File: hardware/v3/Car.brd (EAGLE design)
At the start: 80 x 53.3 mm, 75 parts, among them IC1 PIC24FJ64GB204, IC2 LD117AS50TR, IC3 LD117AS33TR

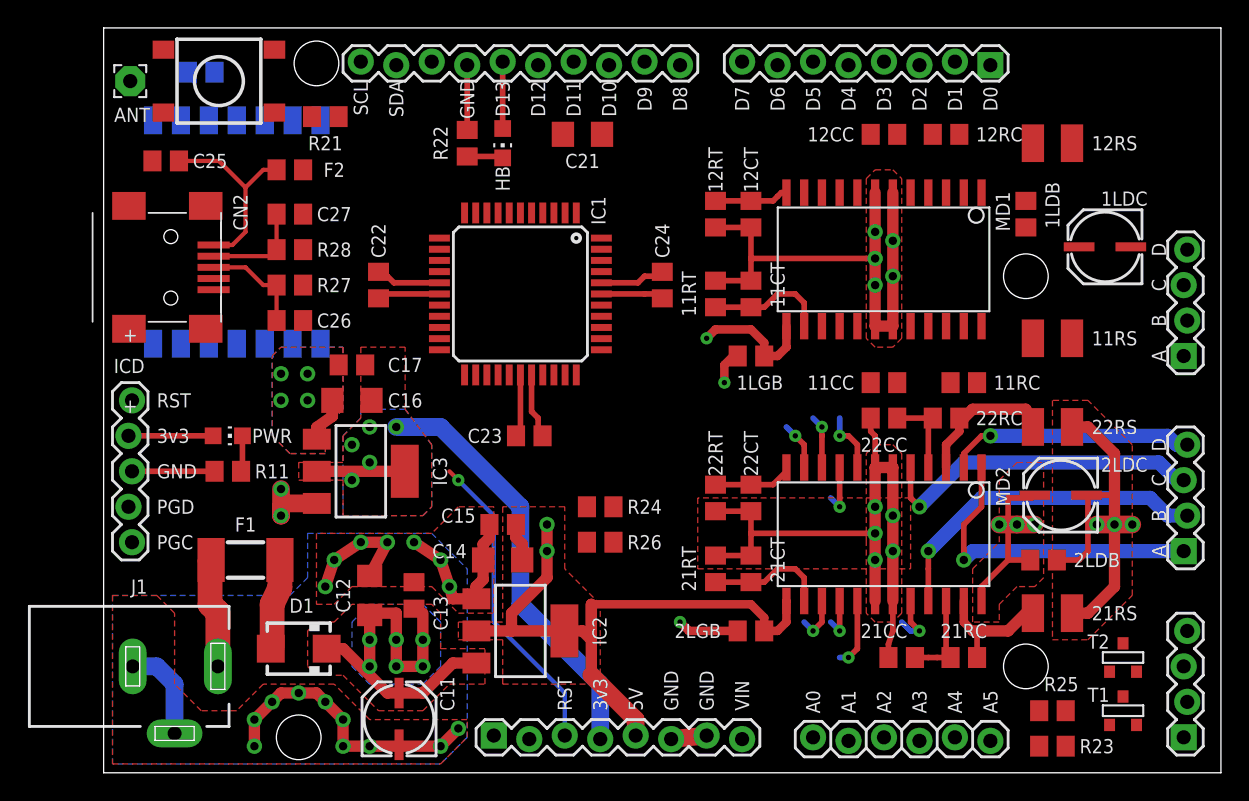
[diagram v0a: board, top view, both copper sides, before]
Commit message: Finished routing power for motor driver 1.
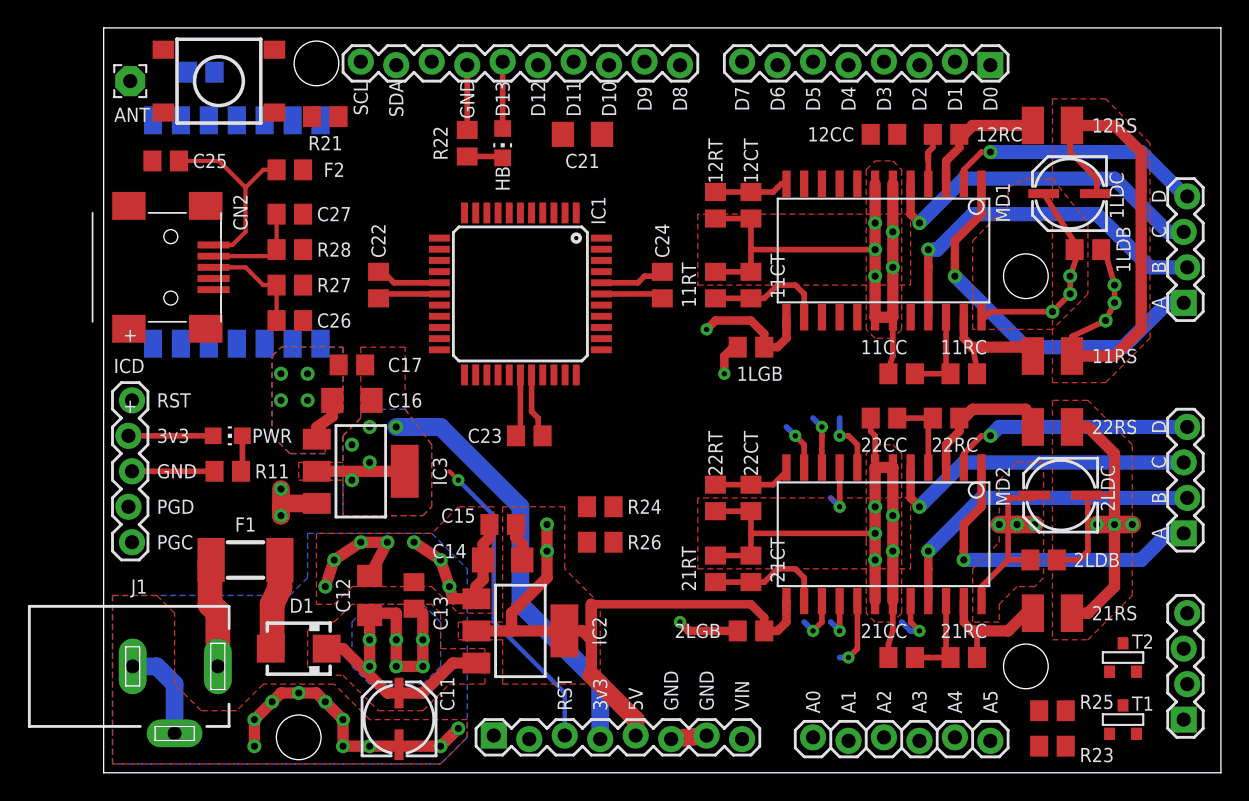
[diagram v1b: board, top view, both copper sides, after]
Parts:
- 11RS, 21RS: value 1 -> 0.5
- moved 1LDB 5.12 mm to (70.5, 37.5), turned to 0 degrees
- moved 1LDC 4.58 mm to (69.2, 41.3)
- moved M1 3.81 mm to (77.5, 33.7)
- moved 11CC 1.42 mm to (57.1, 28.6)
- moved JP1 1.27 mm to (77.5, 3.81)
- moved 11RS 1.27 mm to (67.9, 29.8)
- moved M2 1.27 mm to (77.5, 17.1)
- moved 12RS 1.27 mm to (67.9, 46.4)
- moved MD1 0.64 mm to (55.9, 37.5)
- moved 1LGB 0.64 mm to (46.4, 30.5)
- moved T1 0.64 mm to (73.0, 3.81)
- moved 11CT 0.63 mm to (46.4, 34.9)
- moved 11RC 0.63 mm to (61.6, 28.6)
- moved 11RT 0.63 mm to (43.8, 34.9)
- moved 12CT 0.63 mm to (46.4, 40.6)
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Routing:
- net GND: track 453.9 -> 499.4 mm, vias 36 -> 39
- net N$2: track 0.00 -> 27.2 mm, vias 0 -> 1
- net N$1: track 0.00 -> 26.0 mm, vias 0 -> 1
- net N$4: track 0.00 -> 24.9 mm, vias 0 -> 1
- net N$5: track 0.00 -> 19.0 mm, vias 0 -> 1
- net VIN: track 166.0 -> 179.2 mm, vias 9 -> 12
- net N$35: track 0.00 -> 9.46 mm
- net N$31: track 0.00 -> 8.96 mm
- net N$33: track 0.00 -> 7.36 mm
- net N$34: track 0.00 -> 4.30 mm
- net +5V: track 114.2 -> 114.8 mm
- net N$9: track 23.8 -> 23.3 mm
- net N$8: track 23.2 -> 23.7 mm
- net N$6: track 24.2 -> 23.7 mm

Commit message: Finished routing power lines and other significant signals.
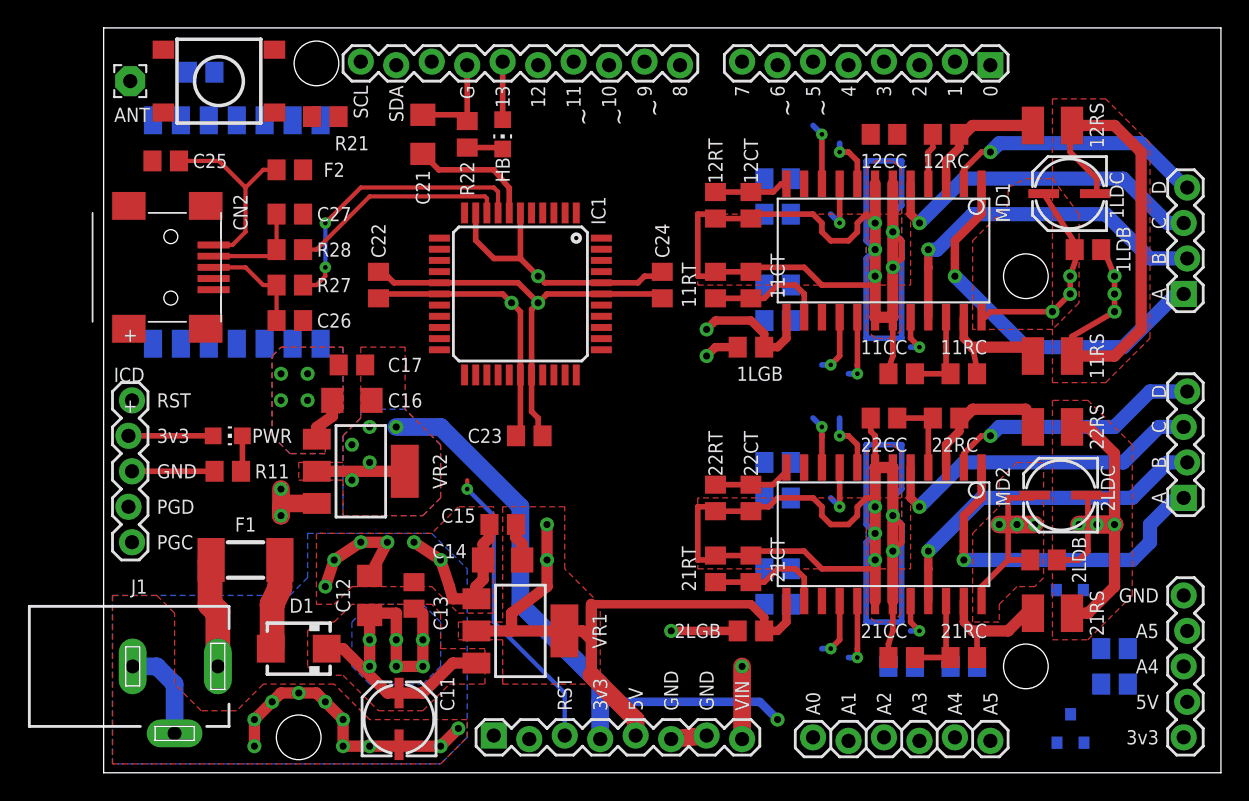
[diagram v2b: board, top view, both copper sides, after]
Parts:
- removed JP1: (no value), SparkFun-Connectors:1X04_LOCK
- added C31, C32, C33, C34: 1n, rcl:C0805
- added PIO: (no value), SparkFun-Connectors:1X05_LOCK
- added R31, R32, R33, R34: 2k, rcl:R0805
- 12RS, 22RS: value 1 -> 0.5
- R23, R25: value 1k -> 10k
- T1, T2: value (none) -> 2N3904
- moved R24 39.0 mm to (72.4, 6.35), flipped to the bottom
- moved R26 37.6 mm to (72.4, 8.89), flipped to the bottom
- moved R23 12.2 mm to (57.1, 7.62), flipped to the bottom, turned to 180 degrees
- moved C21 11.4 mm to (22.9, 45.7), turned to 90 degrees
- moved R25 7.10 mm to (61.6, 7.62), flipped to the bottom, turned to 180 degrees
- moved T2 5.39 mm to (69.2, 12.1), flipped to the bottom, turned to 0 degrees
- moved T1 3.86 mm to (69.2, 3.17), flipped to the bottom
- moved M2 2.54 mm to (77.5, 19.7)
- moved HB 0.63 mm to (28.6, 45.7)
- moved M1 0.63 mm to (77.5, 34.3)
- moved R22 0.63 mm to (26.0, 45.7)
- renumbered IC2 to VR1, IC3 to VR2, JP6 to PWR_IN, JP7 to DIO1, JP8 to DIO2, JP9 to AIO
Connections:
- new net M1_VREF1: C31.1, MD1.15, R31.2
- new net M1_VREF2: C32.1, MD1.11, R32.2
- new net M2_VREF1: C33.1, MD2.15, R33.2
- new net M2_VREF2: C34.1, MD2.11, R34.2
- net +3V3: now also PIO.1
- net +5V: now also PIO.2; no longer JP1.1, R24.2, R26.2
- net A4_PO: now also PIO.3, R24.2; no longer JP1.2, T1.2
- net A5_PO: now also PIO.4, R26.2; no longer JP1.3, T2.2
- net D10/M2_PWM2: now also R34.1; no longer MD2.11
- net D5/M1_PWM1: now also R31.1; no longer MD1.15
- net D6/M1_PWM2: now also R32.1; no longer MD1.11
- net D9/M2_PWM1: now also R33.1; no longer MD2.15
- net GND: now also C31.2, C32.2, C33.2, C34.2, PIO.5, T1.2, T2.2; no longer JP1.4
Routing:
- net GND: track 499.4 -> 695.5 mm
- net +3V3: track 72.6 -> 161.5 mm, vias 5 -> 8
- net +5V: track 114.8 -> 153.4 mm
- net USBD+: track 0.00 -> 20.7 mm, vias 0 -> 2
- net USBD-: track 0.00 -> 15.8 mm
- net N$40: track 0.00 -> 9.05 mm
- net M1_I11: track 0.00 -> 4.68 mm, vias 0 -> 1
- net D3/M1_P2: track 0.00 -> 4.44 mm, vias 0 -> 1
- net D2/M1_P1: track 0.00 -> 4.31 mm, vias 0 -> 1
- net VIN: track 179.2 -> 183.4 mm, vias 12 -> 13
- net M1_I02: track 0.00 -> 3.80 mm, vias 0 -> 1
- net M1_I12: track 0.00 -> 3.71 mm, vias 0 -> 1
- net D10/M2_PWM2: track 3.43 -> 0.00 mm, vias 1 -> 0
- net D9/M2_PWM1: track 3.30 -> 0.00 mm, vias 1 -> 0
- net M1_I01: track 0.00 -> 3.04 mm, vias 0 -> 1
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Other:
- board text added: "0"
- board text added: "1"
- board text added: "10"
- board text added: "11"
- board text added: "12"
- board text added: "13"
- board text added: "2"
- board text added: "3"
- board text added: "4"
- board text added: "5"
- board text added: "6"
- board text added: "7"
- board text added: "8"
- board text added: "9"
- board text added: "G"
- board text added: "~"
- board text removed: "D0"
- board text removed: "D1"
- board text removed: "D10"
- board text removed: "D11"
- board text removed: "D12"
- board text removed: "D13"
- board text removed: "D2"
- board text removed: "D3"
- board text removed: "D4"
- board text removed: "D5"
- board text removed: "D6"
- board text removed: "D7"
- board text removed: "D8"
- board text removed: "D9"

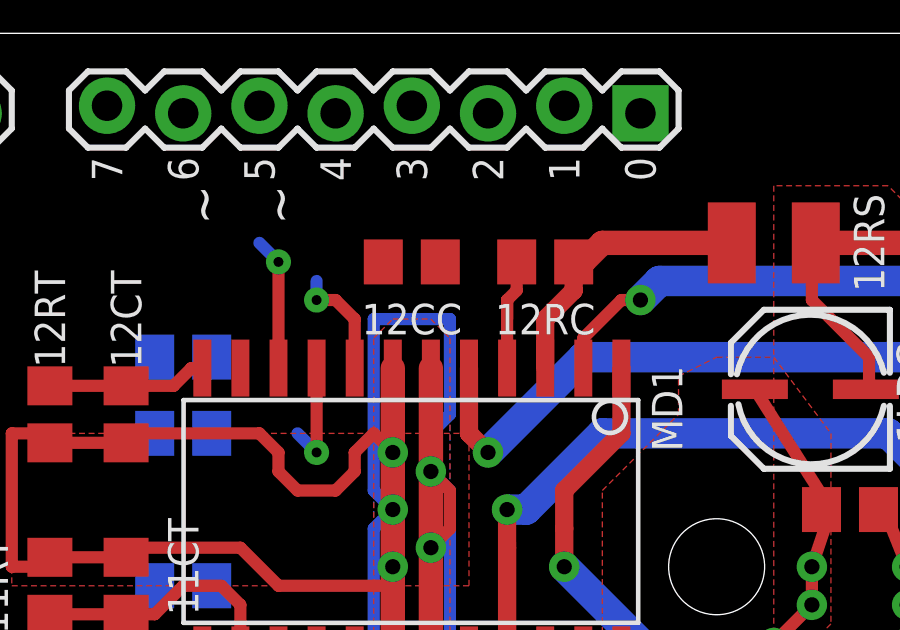
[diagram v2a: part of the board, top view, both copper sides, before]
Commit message: Fixed some part values. Cleaned up schematic and board names/values.
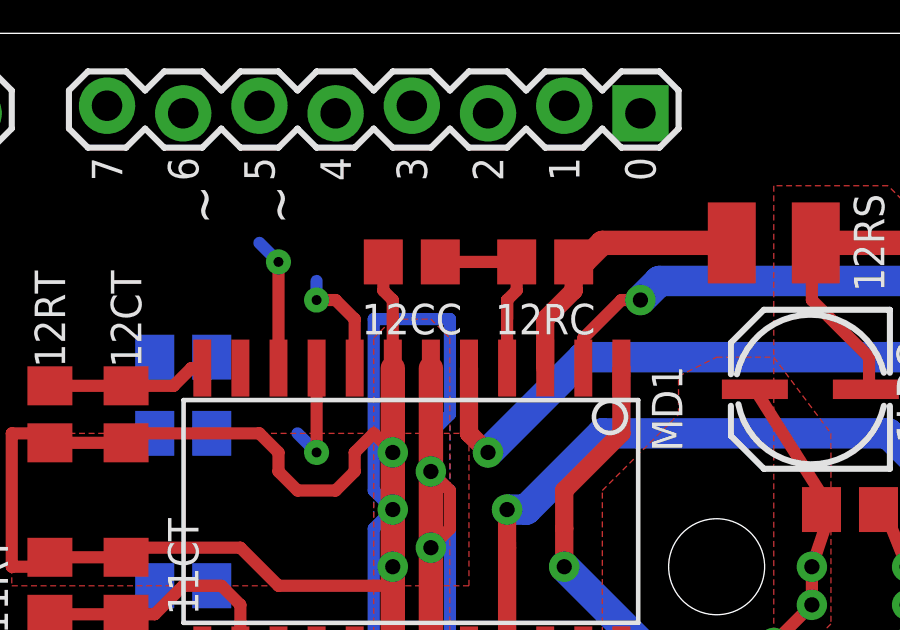
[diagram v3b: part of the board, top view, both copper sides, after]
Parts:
- C31, C32, C33, C34: value 1n -> 100n
- R31, R32, R33, R34: value 2k -> 10k
- renumbered MOUTH to IC2
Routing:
- net GND: track 695.5 -> 699.1 mm
- net N$34: track 4.30 -> 6.85 mm
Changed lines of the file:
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@@
 <attribute name="VALUE" x="47.625" y="33.02" size="1.016" layer="27" rot="R180" align="center"/>
 </element>
-<element name="MOUTH" library="SparkFun-RF" package="RFM12-XXX-S2" value="RFM12" x="9.525" y="38.735" smashed="yes" rot="MR90">
+<element name="IC2" library="SparkFun-RF" package="RFM12-XXX-S2" value="RFM12" x="9.525" y="38.735" smashed="yes" rot="MR90">
 <attribute name="VALUE" x="5.535" y="43.725" size="1.016" layer="28" rot="MR270" align="center"/>
 <attribute name="NAME" x="18.775" y="38.645" size="1.016" layer="26" rot="MR270" align="center"/>
@@
 <attribute name="VALUE" x="80.645" y="1.27" size="1.27" layer="27" rot="R90"/>
 </element>
-<element name="R31" library="rcl" package="R0805" value="2k" x="48.26" y="32.385" smashed="yes" rot="MR180">
+<element name="R31" library="rcl" package="R0805" value="10k" x="48.26" y="32.385" smashed="yes" rot="MR180">
 <attribute name="NAME" x="53.34" y="31.75" size="1.27" layer="26" rot="MR0"/>
 <attribute name="VALUE" x="47.625" y="34.925" size="1.27" layer="28" rot="MR180"/>
 </element>
-<element name="C31" library="rcl" package="C0805" value="1n" x="48.26" y="34.925" smashed="yes" rot="MR0">
+<element name="C31" library="rcl" package="C0805" value="100n" x="48.26" y="34.925" smashed="yes" rot="MR0">
 <attribute name="PN-DK" value="478-1395-1-ND" x="48.26" y="34.925" size="1.778" layer="28" rot="MR0" display="off"/>
 <attribute name="NAME" x="53.34" y="34.29" size="1.27" layer="26" rot="MR0"/>
 <attribute name="VALUE" x="49.53" y="32.385" size="1.27" layer="28" rot="MR0"/>
 </element>
-<element name="R32" library="rcl" package="R0805" value="2k" x="48.26" y="42.545" smashed="yes" rot="MR180">
+<element name="R32" library="rcl" package="R0805" value="10k" x="48.26" y="42.545" smashed="yes" rot="MR180">
 <attribute name="NAME" x="53.34" y="39.37" size="1.27" layer="26" rot="MR0"/>
 <attribute name="VALUE" x="47.625" y="45.085" size="1.27" layer="28" rot="MR180"/>
 </element>
-<element name="C32" library="rcl" package="C0805" value="1n" x="48.26" y="40.005" smashed="yes" rot="MR0">
+<element name="C32" library="rcl" package="C0805" value="100n" x="48.26" y="40.005" smashed="yes" rot="MR0">
 <attribute name="PN-DK" value="478-1395-1-ND" x="48.26" y="40.005" size="1.778" layer="28" rot="MR0" display="off"/>
 <attribute name="NAME" x="53.34" y="41.91" size="1.27" layer="26" rot="MR0"/>
 <attribute name="VALUE" x="49.53" y="37.465" size="1.27" layer="28" rot="MR0"/>
 </element>
-<element name="R33" library="rcl" package="R0805" value="2k" x="48.26" y="12.065" smashed="yes" rot="MR180">
+<element name="R33" library="rcl" package="R0805" value="10k" x="48.26" y="12.065" smashed="yes" rot="MR180">
 <attribute name="NAME" x="53.34" y="11.43" size="1.27" layer="26" rot="MR0"/>
 <attribute name="VALUE" x="47.625" y="14.605" size="1.27" layer="28" rot="MR180"/>
 </element>
-<element name="C33" library="rcl" package="C0805" value="1n" x="48.26" y="14.605" smashed="yes" rot="MR0">
+<element name="C33" library="rcl" package="C0805" value="100n" x="48.26" y="14.605" smashed="yes" rot="MR0">
 <attribute name="PN-DK" value="478-1395-1-ND" x="48.26" y="8.255" size="1.778" layer="28" rot="MR0" display="off"/>
 <attribute name="NAME" x="53.34" y="13.97" size="1.27" layer="26" rot="MR0"/>
 <attribute name="VALUE" x="49.53" y="12.065" size="1.27" layer="28" rot="MR0"/>
 </element>
-<element name="R34" library="rcl" package="R0805" value="2k" x="48.26" y="22.225" smashed="yes" rot="MR180">
+<element name="R34" library="rcl" package="R0805" value="10k" x="48.26" y="22.225" smashed="yes" rot="MR180">
 <attribute name="NAME" x="53.34" y="19.05" size="1.27" layer="26" rot="MR0"/>
 <attribute name="VALUE" x="47.625" y="24.765" size="1.27" layer="28" rot="MR180"/>
 </element>
-<element name="C34" library="rcl" package="C0805" value="1n" x="48.26" y="19.685" smashed="yes" rot="MR0">
+<element name="C34" library="rcl" package="C0805" value="100n" x="48.26" y="19.685" smashed="yes" rot="MR0">
 <attribute name="PN-DK" value="478-1395-1-ND" x="52.705" y="0.635" size="1.778" layer="28" rot="MR0" display="off"/>
 <attribute name="NAME" x="53.34" y="21.59" size="1.27" layer="26" rot="MR0"/>
@@
 <wire x1="59.375" y1="45.72" x2="59.375" y2="44.768" width="0.4064" layer="1"/>
 <wire x1="59.375" y1="44.768" x2="59.056" y2="44.449" width="0.4064" layer="1"/>
-<wire x1="59.375" y1="45.72" x2="56.83" y2="45.72" width="0" layer="19" extent="1-1"/>
+<wire x1="56.83" y1="45.72" x2="59.375" y2="45.72" width="0.4064" layer="1"/>
 </signal>
 <signal name="N$35" class="1">
@@
 </signal>
 <signal name="N$11">
-<contactref element="MOUTH" pad="8"/>
+<contactref element="IC2" pad="8"/>
 <contactref element="ANT" pad="1"/>
 <wire x1="1.905" y1="49.53" x2="3.535" y2="46.725" width="0" layer="19" extent="16-16"/>
 </signal>
 <signal name="D8/RFM_IRQ">
-<contactref element="MOUTH" pad="2"/>
+<contactref element="IC2" pad="2"/>
 <contactref element="IC1" pad="26"/>
 <contactref element="DIO2" pad="1"/>
@@
 </signal>
 <signal name="RFM_CS">
-<contactref element="MOUTH" pad="14"/>
+<contactref element="IC2" pad="14"/>
 <contactref element="IC1" pad="27"/>
 <wire x1="29.045" y1="28.49" x2="15.535" y2="46.725" width="0" layer="19" extent="1-16"/>
@@
 <contactref element="R21" pad="2"/>
 <contactref element="ICD" pad="1"/>
-<contactref element="MOUTH" pad="6"/>
+<contactref element="IC2" pad="6"/>
 <contactref element="IC1" pad="18"/>
 <contactref element="S1" pad="A2"/>
@@
 <vertex x="57.15" y="23.495"/>
 </polygon>
-<contactref element="MOUTH" pad="10"/>
-<contactref element="MOUTH" pad="7"/>
+<contactref element="IC2" pad="10"/>
+<contactref element="IC2" pad="7"/>
 <contactref element="C31" pad="2"/>
 <contactref element="C32" pad="2"/>
@@
 <wire x1="54.61" y1="10.795" x2="54.61" y2="16.51" width="0.4064" layer="16"/>
 <wire x1="54.61" y1="16.51" x2="55.245" y2="17.145" width="0.4064" layer="16"/>
-<wire x1="54.61" y1="43.815" x2="54.93" y2="45.72" width="0" layer="19" extent="1-16"/>
+<wire x1="54.93" y1="45.72" x2="54.93" y2="44.765" width="0.4064" layer="1"/>
+<wire x1="54.93" y1="44.765" x2="55.245" y2="44.45" width="0.4064" layer="1"/>
+<wire x1="55.245" y1="44.45" x2="55.245" y2="42.183" width="0.4064" layer="1"/>
+<wire x1="55.245" y1="42.183" x2="55.246" y2="42.182" width="0.4064" layer="1"/>
+<wire x1="72.39" y1="13.335" x2="77.343" y2="12.7" width="0" layer="19" extent="1-1"/>
 <wire x1="26.035" y1="50.673" x2="26.035" y2="50.8" width="0" layer="19" extent="1-2"/>
 <wire x1="47.31" y1="19.685" x2="46.99" y2="20.32" width="0" layer="19" extent="2-16"/>
@@
 <wire x1="70.1548" y1="13.081" x2="70.485" y2="11.43" width="0" layer="19" extent="1-16"/>
 <wire x1="14.285" y1="32.385" x2="14.605" y2="28.575" width="0" layer="19" extent="1-1"/>
-<wire x1="77.343" y1="12.7" x2="72.39" y2="13.335" width="0" layer="19" extent="1-1"/>
 <wire x1="7.874" y1="34.595" x2="14.285" y2="32.385" width="0" layer="19" extent="1-1"/>
 <wire x1="3.535" y1="30.725" x2="7.874" y2="34.595" width="0" layer="19" extent="1-16"/>
@@
 <signal name="D11/MOSI">
 <contactref element="IC1" pad="36"/>
-<contactref element="MOUTH" pad="12"/>
+<contactref element="IC2" pad="12"/>
 <contactref element="DIO2" pad="4"/>
 <wire x1="35.645" y1="31.89" x2="33.655" y2="50.927" width="0" layer="19" extent="1-1"/>
@@
 <signal name="D12/MISO">
 <contactref element="IC1" pad="37"/>
-<contactref element="MOUTH" pad="1"/>
+<contactref element="IC2" pad="1"/>
 <contactref element="DIO2" pad="5"/>
 <wire x1="35.645" y1="32.69" x2="31.115" y2="50.673" width="0" layer="19" extent="1-1"/>
@@
 <contactref element="IC1" pad="38"/>
 <contactref element="HB" pad="A"/>
-<contactref element="MOUTH" pad="13"/>
+<contactref element="IC2" pad="13"/>
 <contactref element="DIO2" pad="6"/>
 <wire x1="28.575" y1="46.77" x2="28.575" y2="50.927" width="0.4064" layer="1"/>
@@
 <wire x1="24.13" y1="24.765" x2="20.955" y2="24.765" width="1.27" layer="16"/>
 <contactref element="PIO" pad="1"/>
-<contactref element="MOUTH" pad="9"/>
+<contactref element="IC2" pad="9"/>
 <wire x1="35.56" y1="2.413" x2="35.56" y2="1.905" width="0.8128" layer="16"/>
 <wire x1="35.56" y1="1.905" x2="35.56" y2="5.08" width="0.4064" layer="16"/>
